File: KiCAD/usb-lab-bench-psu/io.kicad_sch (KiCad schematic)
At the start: 37 parts, among them J11 Conn_01x03, J12 Conn_01x03, J13 Conn_01x03, J14 Conn_01x12, SW3 RotaryEncoder, SW4 SW_Push, SW5 SW_Push, SW6 SW_Push, SW7 SW_Push, SW8 SW_Push, SW9 SW_Push, U13 TCA9534, U5 LMR16006X

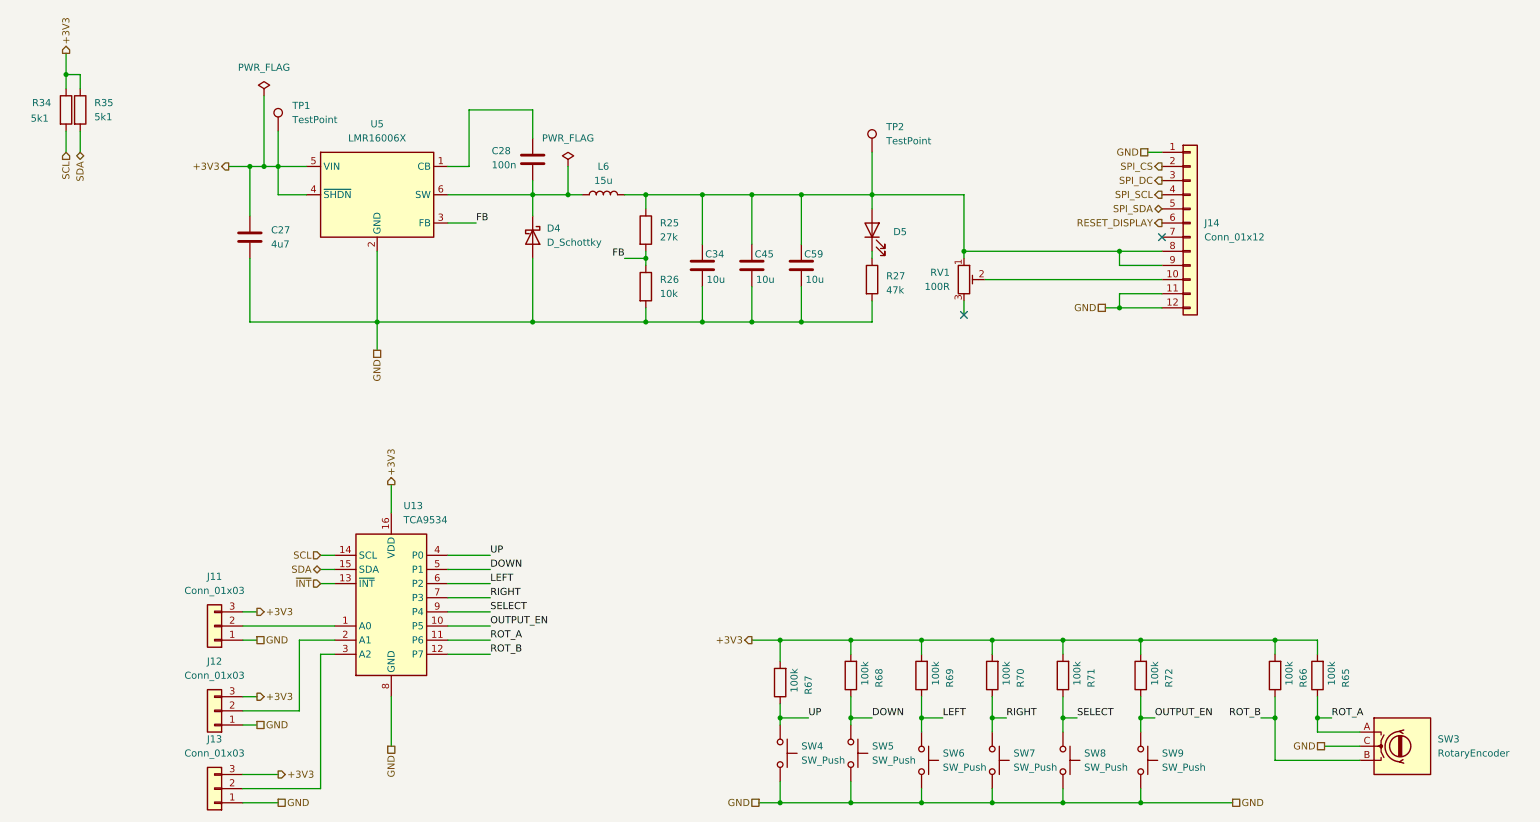
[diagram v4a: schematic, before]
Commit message: added current limiting circuit for USB PD sink, added 2nd buck converter
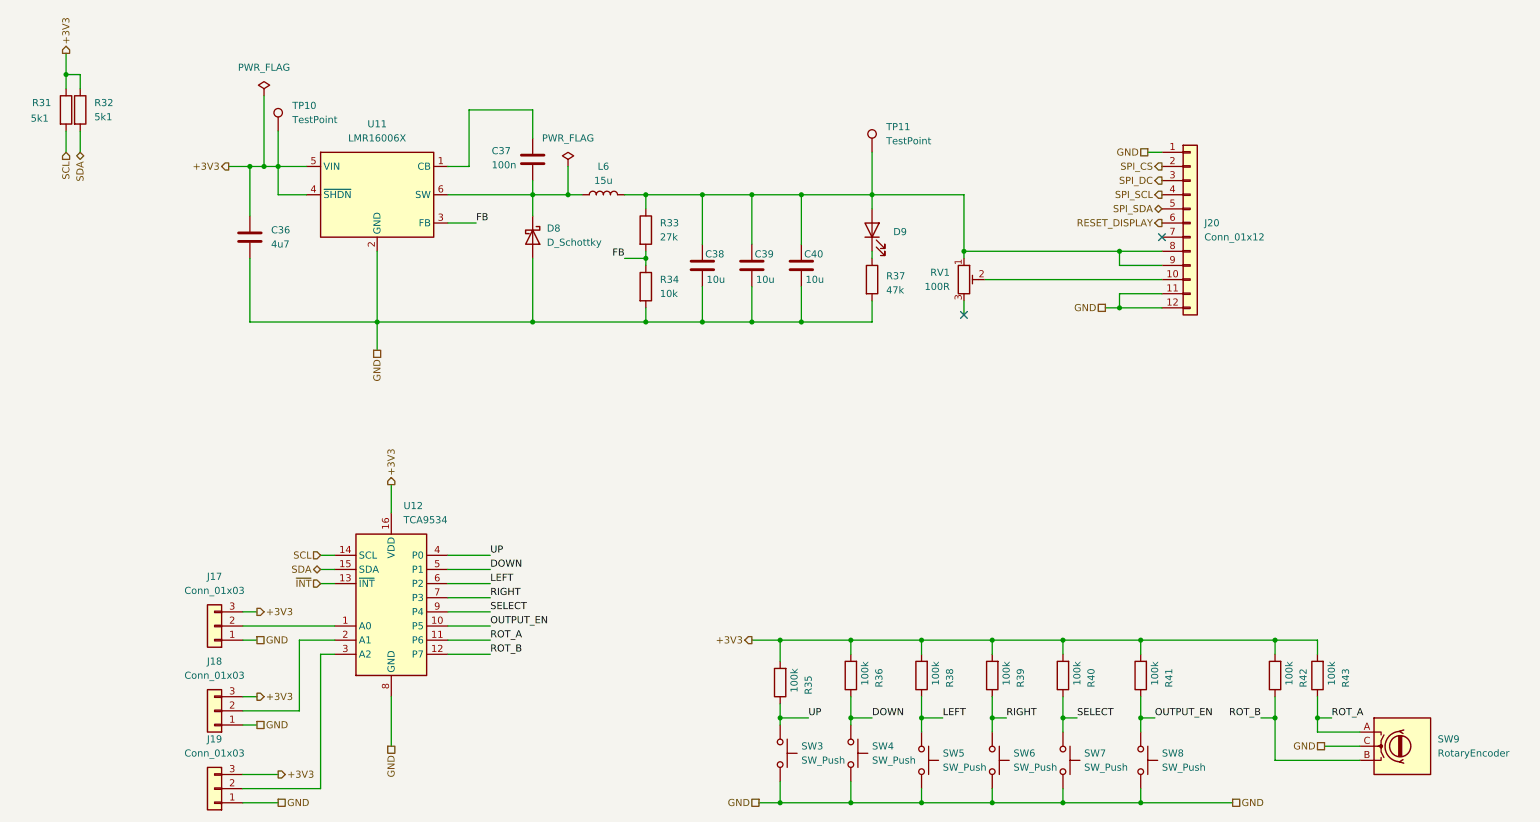
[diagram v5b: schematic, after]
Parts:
- renumbered C27 to C36, C28 to C37, C34 to C38, C45 to C39, C59 to C40, D4 to D8, D5 to D9, J11 to J17, J12 to J18, J13 to J19, J14 to J20, R34 to R31, R35 to R32, R25 to R33, R26 to R34, R67 to R35, R68 to R36, R27 to R37, R69 to R38, R70 to R39, R71 to R40, R72 to R41, R66 to R42, R65 to R43, SW4 to SW3, SW5 to SW4, SW6 to SW5, SW7 to SW6, SW8 to SW7, SW9 to SW8, SW3 to SW9, TP1 to TP10, TP2 to TP11, U5 to U11, U13 to U12

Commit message: tweaked design of current limiter, added GPIO expander to USB-PD circuit
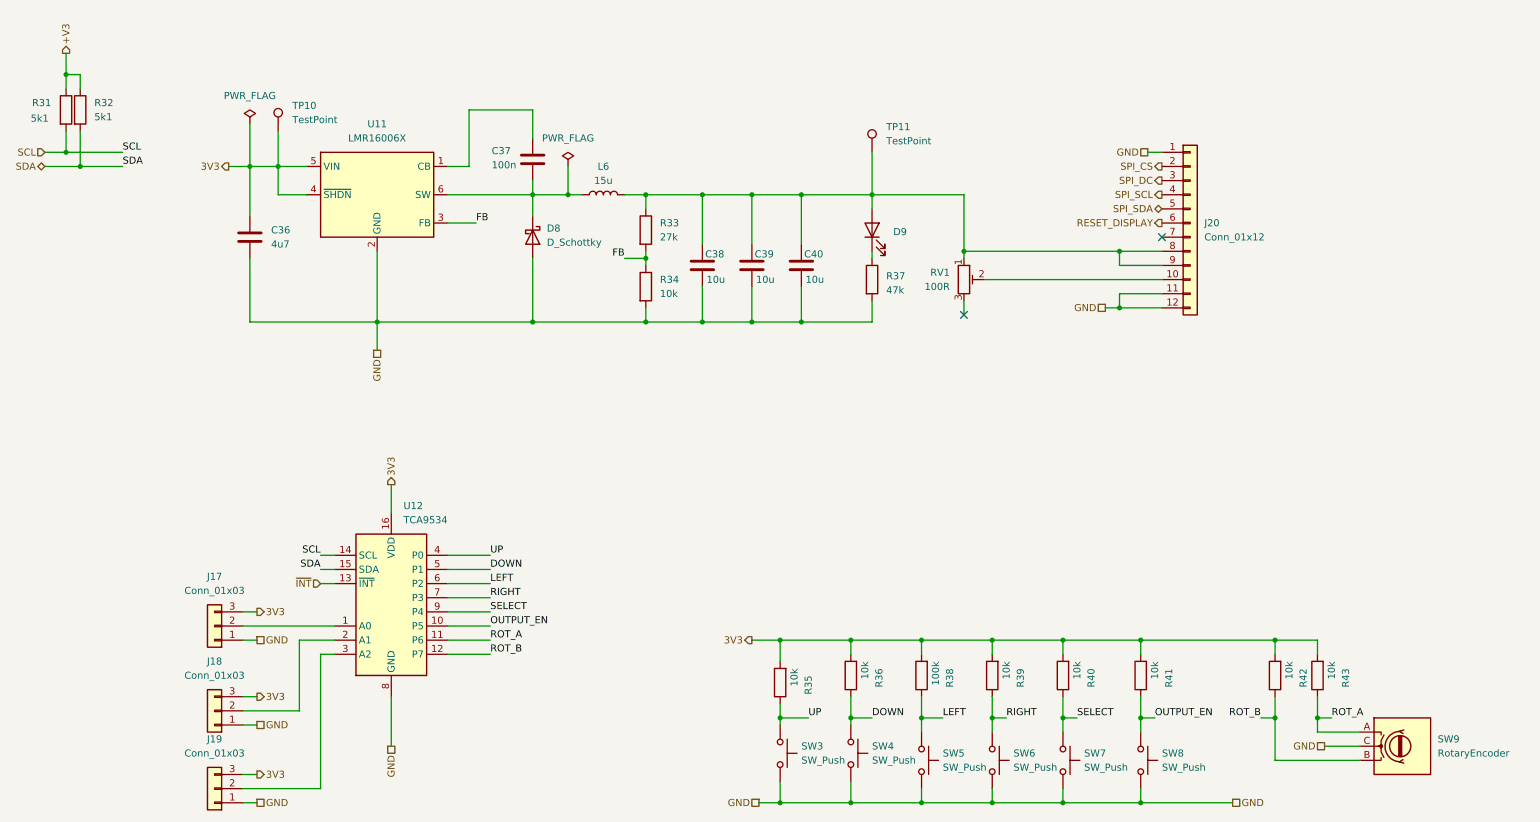
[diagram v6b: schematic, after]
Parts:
- R35, R36, R39, R40, R41, R42, R43: value 100k -> 10k
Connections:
- net +3V3 renamed 3V3
- net 3V3: no longer R31.1, R32.1
- new net +V3: R31.1, R32.1
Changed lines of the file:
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@@
 	(paper "A4")
 	(junction
+		(at 33.02 45.72)
+		(diameter 0)
+		(color 0 0 0 0)
+	)
+	(junction
 		(at 171.45 160.02)
 		(diameter 0)
@@
 	)
 	(junction
-		(at 66.04 45.72)
-		(diameter 0)
-		(color 0 0 0 0)
-	)
-	(junction
 		(at 219.71 60.96)
 		(diameter 0)
@@
 	)
 	(junction
+		(at 30.48 43.18)
+		(diameter 0)
+		(color 0 0 0 0)
+	)
+	(junction
 		(at 184.15 144.78)
 		(diameter 0)
@@
 	(wire
 		(pts
-			(xy 66.04 33.02) (xy 66.04 45.72)
-		)
-		(stroke
-			(width 0)
-			(type default)
-		)
-	)
-	(wire
-		(pts
-			(xy 66.04 45.72) (xy 68.58 45.72)
+			(xy 63.5 38.1) (xy 63.5 45.72)
 		)
 		(stroke
@@
 	(wire
 		(pts
-			(xy 62.23 154.94) (xy 68.58 154.94)
+			(xy 62.23 154.94) (xy 64.77 154.94)
 		)
 		(stroke
@@
 	(wire
 		(pts
-			(xy 33.02 39.37) (xy 33.02 43.18)
-		)
-		(stroke
-			(width 0)
-			(type default)
-		)
-	)
-	(wire
-		(pts
 			(xy 76.2 157.48) (xy 62.23 157.48)
 		)
@@
 	(wire
 		(pts
+			(xy 33.02 39.37) (xy 33.02 45.72)
+		)
+		(stroke
+			(width 0)
+			(type default)
+		)
+	)
+	(wire
+		(pts
 			(xy 63.5 73.66) (xy 86.36 73.66)
 		)
@@
 	(wire
 		(pts
-			(xy 63.5 45.72) (xy 66.04 45.72)
+			(xy 63.5 45.72) (xy 68.58 45.72)
 		)
 		(stroke
@@
 	(wire
 		(pts
-			(xy 62.23 160.02) (xy 68.58 160.02)
+			(xy 62.23 160.02) (xy 64.77 160.02)
 		)
 		(stroke
@@
 	(wire
 		(pts
+			(xy 26.67 43.18) (xy 30.48 43.18)
+		)
+		(stroke
+			(width 0)
+			(type default)
+		)
+	)
+	(wire
+		(pts
 			(xy 106.68 133.35) (xy 99.06 133.35)
 		)
@@
 	(wire
 		(pts
+			(xy 26.67 45.72) (xy 33.02 45.72)
+		)
+		(stroke
+			(width 0)
+			(type default)
+		)
+	)
+	(wire
+		(pts
 			(xy 196.85 133.35) (xy 196.85 130.81)
 		)
@@
 	(wire
 		(pts
+			(xy 30.48 43.18) (xy 40.64 43.18)
+		)
+		(stroke
+			(width 0)
+			(type default)
+		)
+	)
+	(wire
+		(pts
 			(xy 76.2 120.65) (xy 78.74 120.65)
 		)
@@
 	(wire
 		(pts
+			(xy 33.02 45.72) (xy 40.64 45.72)
+		)
+		(stroke
+			(width 0)
+			(type default)
+		)
+	)
+	(wire
+		(pts
 			(xy 153.67 130.81) (xy 158.75 130.81)
 		)
@@
 		)
 	)
+	(label "SCL"
+		(at 76.2 115.57 180)
+		(effects
+			(font
+				(size 1.27 1.27)
+			)
+			(justify right bottom)
+		)
+	)
 	(label "DOWN"
 		(at 175.26 144.78 0)
@@
 		)
 	)
+	(label "SDA"
+		(at 40.64 45.72 0)
+		(effects
+			(font
+				(size 1.27 1.27)
+			)
+			(justify left bottom)
+		)
+	)
 	(label "SELECT"
 		(at 106.68 125.73 0)
@@
 		)
 	)
+	(label "SDA"
+		(at 76.2 118.11 180)
+		(effects
+			(font
+				(size 1.27 1.27)
+			)
+			(justify right bottom)
+		)
+	)
 	(label "OUTPUT_EN"
 		(at 106.68 128.27 0)
@@
 		)
 	)
+	(label "SCL"
+		(at 40.64 43.18 0)
+		(effects
+			(font
+				(size 1.27 1.27)
+			)
+			(justify left bottom)
+		)
+	)
 	(label "ROT_A"
 		(at 257.81 144.78 0)
@@
 		)
 	)
-	(hierarchical_label "+3V3"
+	(hierarchical_label "3V3"
 		(shape output)
 		(at 88.9 102.87 90)
@@
 		)
 	)
-	(hierarchical_label "SDA"
-		(shape bidirectional)
-		(at 76.2 118.11 180)
-		(effects
-			(font
-				(size 1.27 1.27)
-			)
-			(justify right)
-		)
-	)
 	(hierarchical_label "SCL"
 		(shape input)
-		(at 30.48 43.18 270)
+		(at 26.67 43.18 180)
 		(effects
 			(font
@@
 		)
 	)
-	(hierarchical_label "+3V3"
+	(hierarchical_label "+V3"
 		(shape output)
 		(at 30.48 25.4 90)
@@
 		)
 	)
-	(hierarchical_label "+3V3"
+	(hierarchical_label "3V3"
 		(shape output)
-		(at 68.58 154.94 0)
+		(at 64.77 154.94 0)
 		(effects
 			(font
@@
 		)
 	)
-	(hierarchical_label "+3V3"
+	(hierarchical_label "3V3"
 		(shape output)
 		(at 59.69 45.72 180)
@@
 	(hierarchical_label "SDA"
 		(shape bidirectional)
-		(at 33.02 43.18 270)
+		(at 26.67 45.72 180)
 		(effects
 			(font
@@
 		)
 	)
-	(hierarchical_label "+3V3"
+	(hierarchical_label "3V3"
 		(shape output)
 		(at 64.77 140.97 0)
@@
 		)
 	)
-	(hierarchical_label "+3V3"
+	(hierarchical_label "3V3"
 		(shape output)
 		(at 153.67 130.81 180)
@@
 	(hierarchical_label "GND"
 		(shape passive)
-		(at 68.58 160.02 0)
+		(at 64.77 160.02 0)
 		(effects
 			(font
@@
 		)
 	)
-	(hierarchical_label "+3V3"
+	(hierarchical_label "3V3"
 		(shape output)
 		(at 64.77 125.73 0)
@@
 		)
 	)
-	(hierarchical_label "SCL"
-		(shape input)
-		(at 76.2 115.57 180)
-		(effects
-			(font
-				(size 1.27 1.27)
-			)
-			(justify right)
-		)
-	)
 	(hierarchical_label "SPI_SDA"
 		(shape bidirectional)
@@
 			)
 		)
-		(property "Value" "100k"
+		(property "Value" "10k"
 			(at 212.09 134.62 90)
 			(effects
@@
 			)
 		)
-		(property "Value" "100k"
+		(property "Value" "10k"
 			(at 199.39 134.62 90)
 			(effects
@@
 			)
 		)
-		(property "Value" "100k"
+		(property "Value" "10k"
 			(at 161.29 135.89 90)
 			(effects
@@
 			)
 		)
-		(property "Value" "100k"
+		(property "Value" "10k"
 			(at 173.99 134.62 90)
 			(effects
@@
 			)
 		)
-		(property "Value" "100k"
+		(property "Value" "10k"
 			(at 250.19 134.62 90)
 			(effects
@@
 	(symbol
 		(lib_id "power:PWR_FLAG")
-		(at 66.04 33.02 0)
+		(at 63.5 38.1 0)
 		(unit 1)
 		(exclude_from_sim no)
@@
 		(fields_autoplaced yes)
 		(property "Reference" "#FLG09"
-			(at 66.04 31.115 0)
+			(at 63.5 36.195 0)
 			(effects
 				(font
@@
 		)
 		(property "Value" "PWR_FLAG"
-			(at 66.04 27.94 0)
+			(at 63.5 33.02 0)
 			(effects
 				(font
@@
 		)
 		(property "Footprint" ""
-			(at 66.04 33.02 0)
+			(at 63.5 38.1 0)
 			(effects
 				(font
@@
 		)
 		(property "Datasheet" "~"
-			(at 66.04 33.02 0)
+			(at 63.5 38.1 0)
 			(effects
 				(font
@@
 		)
 		(property "Description" "Special symbol for telling ERC where power comes from"
-			(at 66.04 33.02 0)
+			(at 63.5 38.1 0)
 			(effects
 				(font
@@
 			)
 		)
-		(property "Value" "100k"
+		(property "Value" "10k"
 			(at 226.06 134.62 90)
 			(effects
@@
 			)
 		)
-		(property "Value" "100k"
+		(property "Value" "10k"
 			(at 257.81 134.62 90)
 			(effects
